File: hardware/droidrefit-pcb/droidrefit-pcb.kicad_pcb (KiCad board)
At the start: 2 copper layers, 100 x 70 mm, 30 parts, among them J1 USB-C 5V in, J2 SERVO SIG/+5V/GND, J3 NEOPIXEL JST-SH, J5 SPEAKER 4-8ohm, Q1 P-MOSFET revpol, U1 ESP32-DevKit-30, U2 DFPlayer-Mini, U3 74AHCT1G125

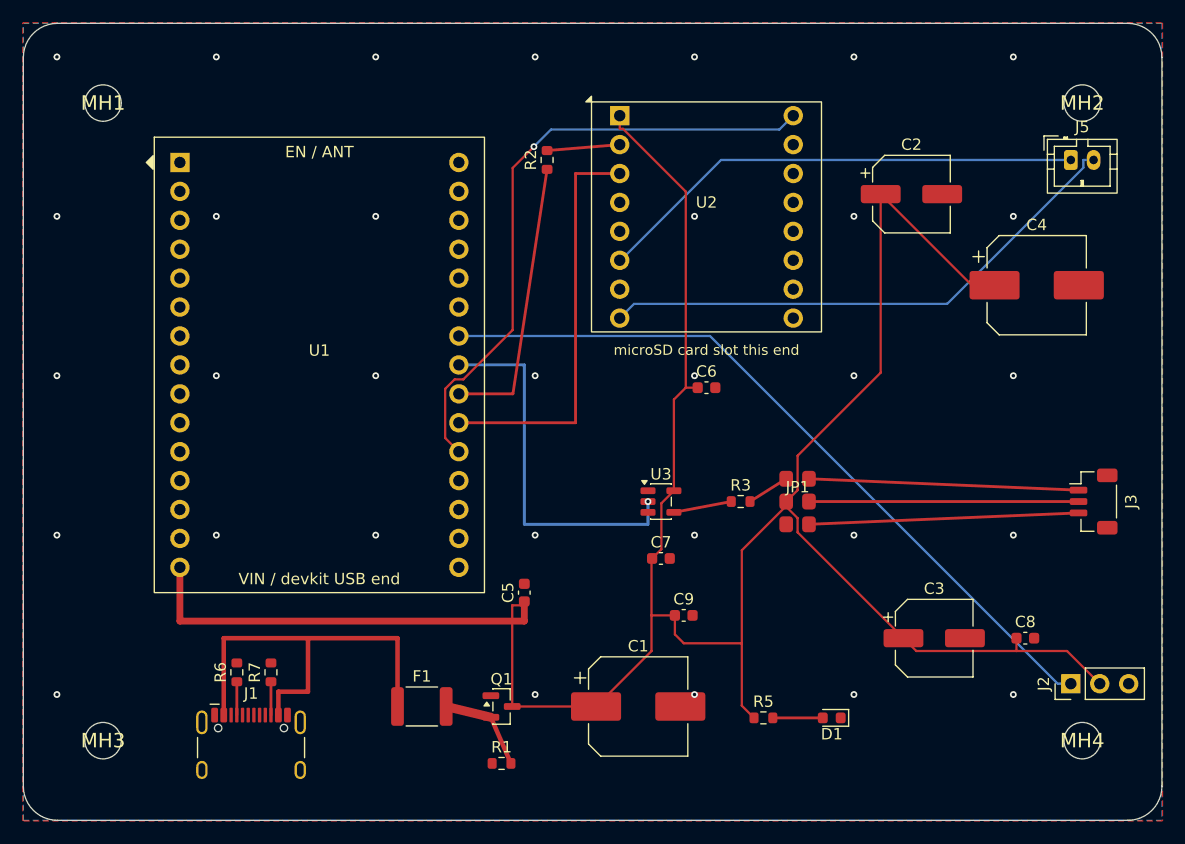
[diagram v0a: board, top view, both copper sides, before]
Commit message: PCB: add buttons/buzzer/OLED/UART headers, fix JP1 default pinout
droidrefit-pcb respin closing gaps DESIGN.md had already speced but never
drawn into the schematic/board:

- New J6 (BUTTONS, 1x4: GND/IO32/IO33/IO25), J7 (BUZZER, 1x2: IO27 via a
  new R8 100ohm series/GND), J8 (OLED I2C, 1x4: 3V3/GND/SDA/SCL, with new
  R9/R10 4.7k pull-ups to 3V3), J9 (UART0 ACCESS, 1x4: 3V3/GND/TX0/RX0).
  All four wired straight to U1's existing free socket pins per the pin
  assignments DESIGN.md's own Connectors/firmware-pin-map tables already
  committed to. All dnp+hand-solder like J2/J5 (2.54mm headers, not
  JLC-placed); R8/R9/R10 are real JLC-placed SMD 0603s.
- Fixed JP1 (NeoPixel pin-order solder-bridge field): shipped default was
  DIN-P1/V+-P2/GND-P3, but this session's NeoPixel bring-up empirically
  confirmed the real dome connector is GND-pin1/V+-pin2/Signal-pin3 -- DIN
  and GND were swapped from the shipped default. Remapped which J3 pin each
  bridge pad reaches so the same-row, no-cut default now matches reality.
- Board: placed + routed all new nets (mostly by hand, Freerouting for the
  denser fan-outs), GND pour refilled to pick up the new pads. ERC clean
  (0 errors, same 3 pre-existing symbol-mismatch warnings as before). DRC:
  down to 1 residual error (a zone-clearance short at JP1's own bare/DNP
  bridge-field pads, reproduced across multiple routing strategies -- looks
  like a zone-fill edge case in that one tightly-packed 6-pad SMD cluster,
  not a connectivity mistake; flagged in DESIGN.md/fab/README.md for a
  quick GUI nudge-and-refill before ordering) plus the same 13 pre-existing
  cosmetic warnings as before.
- Deleted the unused, never-instantiated 74xx:74AHCT125 (quad) and
  Connector:Barrel_Jack symbol-library leftovers from the schematic.
- Regenerated the full fab package (gerbers/drill/BOM-full/BOM-JLC/
  CPL-JLC/README) -- BOM-JLC/CPL-JLC now 16 lines/24 designators (was
  11/17). LCSC part numbers for R8/R9/R10 still TBD, not guessed her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
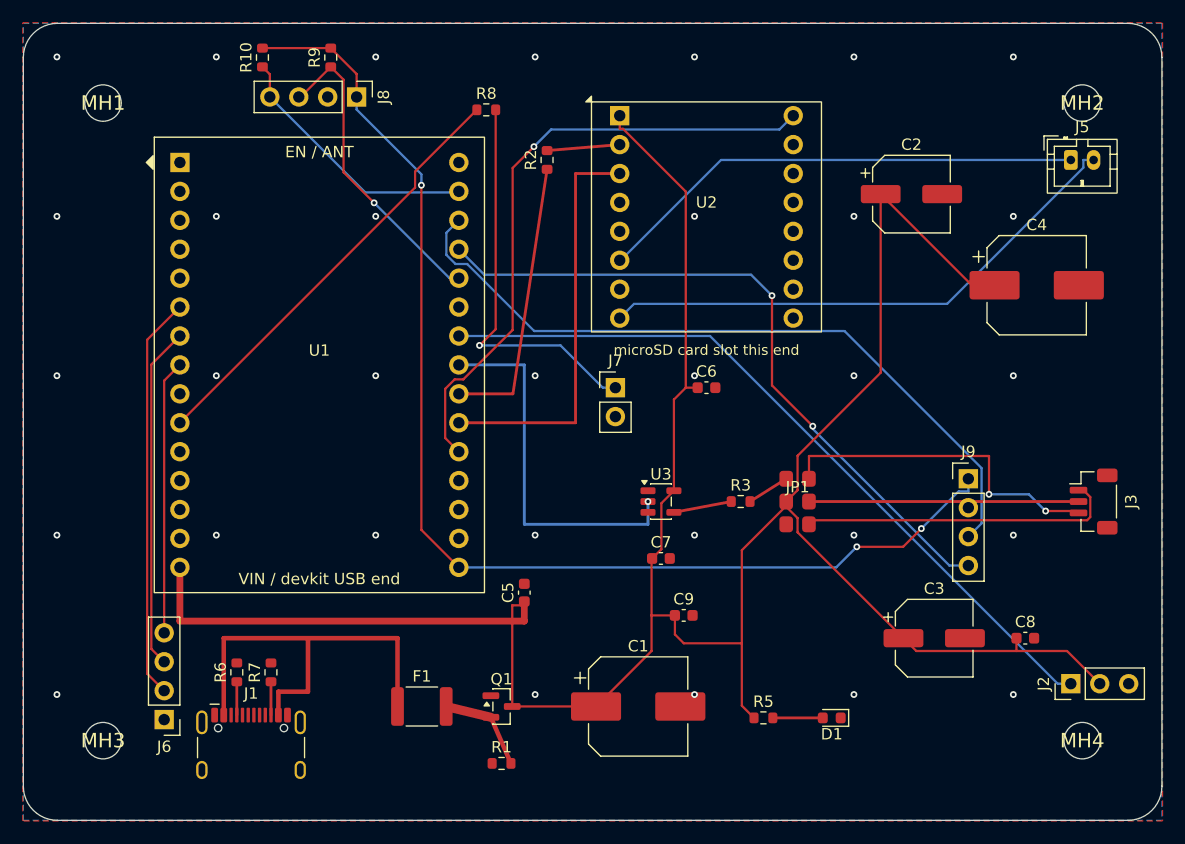
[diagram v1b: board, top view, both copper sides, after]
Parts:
- added J6: BUTTONS, Connector_PinHeader_2.54mm:PinHeader_1x04_P2.54mm_Vertical, F.Cu at (12.4, 61.1)
- added J7: BUZZER, Connector_PinHeader_2.54mm:PinHeader_1x02_P2.54mm_Vertical, F.Cu at (52.0, 32.0)
- added J8: OLED I2C, Connector_PinHeader_2.54mm:PinHeader_1x04_P2.54mm_Vertical, F.Cu at (29.3, 6.46)
- added J9: UART0 ACCESS, Connector_PinHeader_2.54mm:PinHeader_1x04_P2.54mm_Vertical, F.Cu at (83.0, 40.0)
- added R10: 4.7k, Resistor_SMD:R_0603_1608Metric, F.Cu at (21.0, 3.00)
- added R8: 100, Resistor_SMD:R_0603_1608Metric, F.Cu at (40.7, 7.60)
- added R9: 4.7k, Resistor_SMD:R_0603_1608Metric, F.Cu at (27.0, 3.00)
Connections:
- JP1 pad 4: NPX_P1 -> NPX_P3
- JP1 pad 6: NPX_P3 -> NPX_P1
- U1 pad 10: (no net) -> BUZZER_IO27
- U1 pad 17: (no net) -> I2C_SCL
- U1 pad 18: (no net) -> UART0_TX0
- U1 pad 19: (no net) -> UART0_RX0
- U1 pad 20: (no net) -> I2C_SDA
- U1 pad 30: +3V3 -> 3V3
- U1 pad 6: (no net) -> BTN_UP
- U1 pad 7: (no net) -> BTN_DOWN
- U1 pad 8: (no net) -> BTN_SND
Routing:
- net 3V3: track 0.00 -> 104.9 mm, vias 0 -> 3
- net UART0_TX0: track 0.00 -> 64.8 mm
- net UART0_RX0: track 0.00 -> 61.0 mm, vias 0 -> 2
- net BUZZER_IO27: track 0.00 -> 38.3 mm
- net BTN_UP: track 0.00 -> 35.5 mm
- net BUZZER_PWM: track 0.00 -> 34.8 mm, vias 0 -> 1
- net BTN_DOWN: track 0.00 -> 30.1 mm
- net I2C_SDA: track 0.00 -> 27.6 mm, vias 0 -> 1
- net BTN_SND: track 0.00 -> 24.1 mm
- net I2C_SCL: track 0.00 -> 23.0 mm
- net NPX_P3: track 23.7 -> 29.7 mm, vias 0 -> 2
- net NPX_P1: track 23.7 -> 28.0 mm

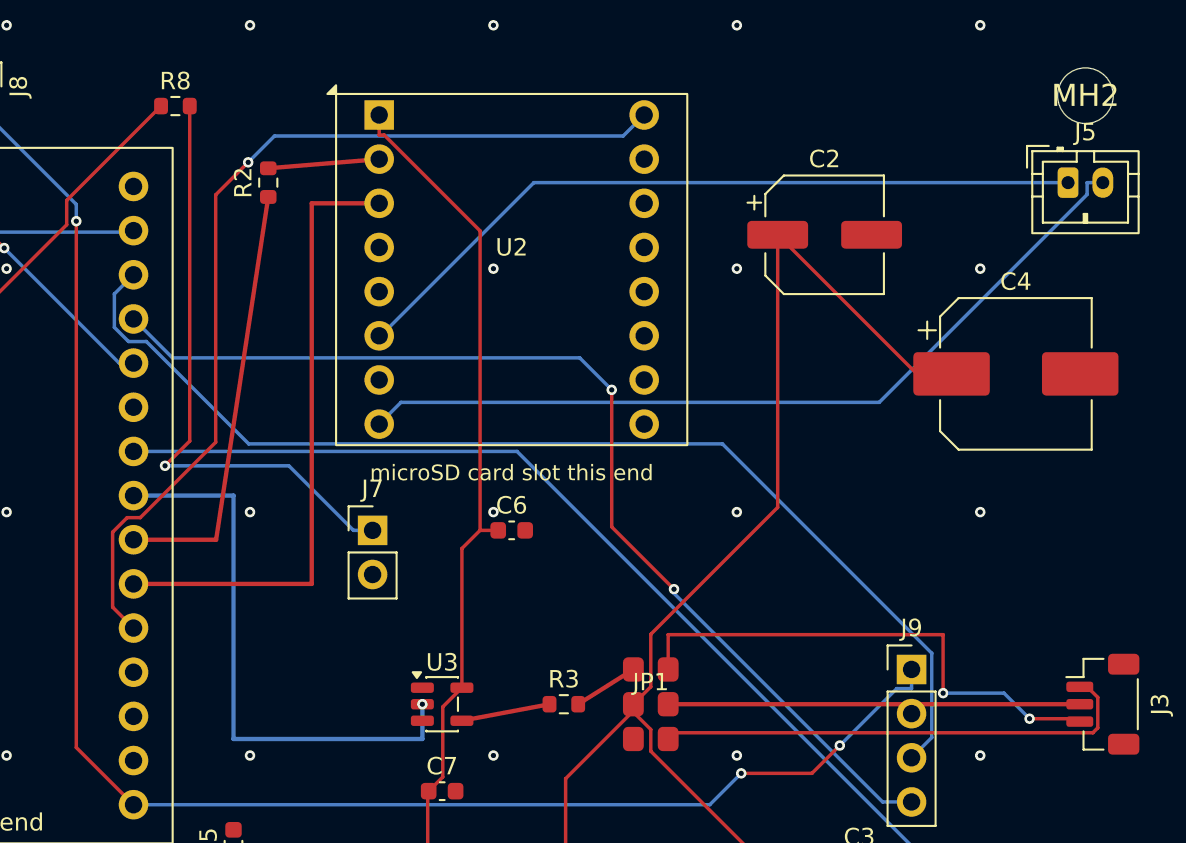
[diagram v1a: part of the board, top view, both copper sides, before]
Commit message: PCB: move J7 off the microSD card path, reroute NPX_P2 around J9 -> 0 DRC errors
Follow-up to the header respin, two fixes:

- J7 (buzzer header) was auto-placed at (52,32), directly in the DFPlayer's
  microSD card insertion/ejection path -- ~3mm south of the SD-slot edge,
  THT pins tall enough to foul a card or a plugged-in wire. Moved to
  (46.25,40), west of the card corridor; BUZZER_PWM re-routed.
- The residual GND/NPX_P2 DRC short was J9 sitting in the JP1->J3 NeoPixel
  bundle: the straight NPX_P2 run at y=42 clipped J9's GND pad at (83,42.54).
  Rerouting P1/P3 around J9 by hand earlier had left P2 straight through.
  Let Freerouting route NPX_P2 (as it already had for P1); that also
  cleared the JP1 bridge-field zone-clearance sliver.

Board is now 0 DRC errors + the same 12 pre-existing cosmetic warnings.
Fab package (gerbers/drill/zip/CPL) regenerated for the new J7 silk
position. BOM unchanged. R8/R9/R10 LCSC part numbers still TBD.

Co-Authored-By: Claude Sonnet 5 <noreply@anthropic.com>
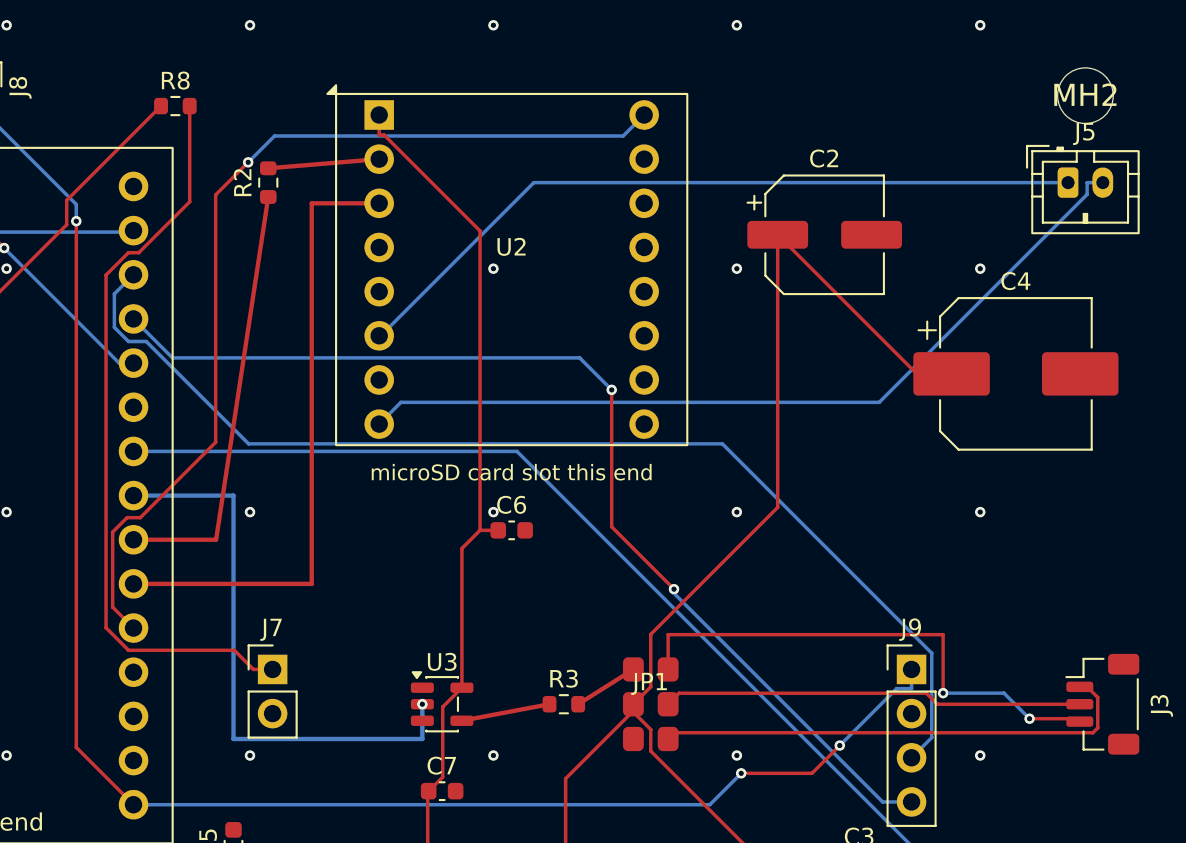
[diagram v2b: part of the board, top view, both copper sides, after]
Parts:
- moved J7 9.85 mm to (46.2, 40.0)
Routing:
- net BUZZER_PWM: track 34.8 -> 42.9 mm, vias 1 -> 0
- net NPX_P2: track 23.7 -> 24.2 mm

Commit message: PCB: move the 4 M3 mounting holes tighter into the corners
The 7mm-inset positions had MH2's keepout ring overlapping J5's courtyard
(a pre-existing body_overlap) and MH3/MH4 crowding the new J6 buttons
header / the J2 servo header -- an M3 screw + washer at those corners would
have fought a plugged-in connector.

Moved all 4 to a symmetric 91 x 61 mm pattern, 4.5 mm in from each edge
(4.5/4.5, 95.5/4.5, 4.5/65.5, 95.5/65.5). Now ~4mm clearance from a washer
edge to the nearest connector pad at every corner. All mechanical
overlaps gone; still 0 DRC errors. Enclosure is 3D-printed and designed
around the holes, so the asymmetry-vs-components tradeoff went to
clearance. Drill file + gerbers + zip regenerated.

Co-Authored-By: Claude Sonnet 5 <noreply@anthropic.com>
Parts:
- moved MH1 3.54 mm to (4.50, 4.50)
- moved MH2 3.54 mm to (95.5, 4.50)
- moved MH3 3.54 mm to (4.50, 65.5)
- moved MH4 3.54 mm to (95.5, 65.5)
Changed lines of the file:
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@@
 	(footprint "MountingHole:MountingHole_3.2mm"
 		(layer "F.Cu")
-		(at 7 63)
+		(at 4.5 65.5)
 		(property "Reference" "MH3"
 			(at 0 0 0)
@@
 	(footprint "MountingHole:MountingHole_3.2mm"
 		(layer "F.Cu")
-		(at 7 7)
+		(at 4.5 4.5)
 		(property "Reference" "MH1"
 			(at 0 0 0)
@@
 	(footprint "MountingHole:MountingHole_3.2mm"
 		(layer "F.Cu")
-		(at 93 7)
+		(at 95.5 4.5)
 		(property "Reference" "MH2"
 			(at 0 0 0)
@@
 	(footprint "MountingHole:MountingHole_3.2mm"
 		(layer "F.Cu")
-		(at 93 63)
+		(at 95.5 65.5)
 		(property "Reference" "MH4"
 			(at 0 0 0)

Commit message: PCB: explicit GND trace to J7 pin 2
KiCad GUI DRC flagged "Zone [GND] on F.Cu, priority 0 - missing
connections" -- J7's GND pad, now sitting in the dense U1<->U2 channel
after the SD-card-path move, isn't reliably reached by the GND pour on
either layer in that tight pocket (the swig-backend DRC didn't catch it;
the GUI's fill engine does). Added a short explicit GND trace from J7/2 to
C5/2 so it no longer depends on the pour squeezing in there.

Still 0 DRC errors here. Refill zones in the KiCad GUI (Edit -> Fill All
Zones / B) after opening -- the swig zone fill and KiCad 9's GUI fill
don't always agree, and the GUI's is authoritative.

Co-Authored-By: Claude Sonnet 5 <noreply@anthropic.com>
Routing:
- net GND: track 0.00 -> 7.05 mm
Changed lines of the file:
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@@
 		)
 		(property "Value" "MountingHole_3.2mm"
-			(at -4.5 -4.5 270)
+			(at 0 -15.5 270)
 			(layer "F.Fab")
 			(effects
@@
 		)
 		(property "Value" "MountingHole_3.2mm"
-			(at -5 6 90)
+			(at 0 14 90)
 			(layer "F.Fab")
 			(effects
@@
 		)
 		(property "Value" "MountingHole_3.2mm"
-			(at -5 -5 0)
+			(at -14 0 0)
 			(layer "F.Fab")
 			(effects
@@
 		)
 		(property "Value" "MountingHole_3.2mm"
-			(at -4 4.5 0)
+			(at -14 0 0)
 			(layer "F.Fab")
 			(effects
@@
 		(net "CC2")
 	)
+	(segment
+		(start 46.25 42.54)
+		(end 44 49.225)
+		(width 0.25)
+		(layer "F.Cu")
+		(net "GND")
+	)
 	(via

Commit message: PCB: GND stitching via to reconnect an isolated F.Cu pour island
kicad-cli DRC (--refill-zones, the same engine as the GUI) showed the real
issue behind the "Zone [GND] on F.Cu missing connections" the swig-backend
DRC kept missing: the F.Cu GND pour was fragmenting into islands. One
island, walled off by the VBUS_IN/CC1/CC2 traces around J1, held R6/R7's
GND pads (SMD, F.Cu-only) with no path back to the net. Added a GND
stitching via at (20.25,56) inside that island, tying it to the
continuous B.Cu GND pour.

kicad-cli DRC now: 0 errors, 0 unconnected items. Zone fill regenerated
with KiCad's own engine (--save-board) so the on-disk fill matches the GUI.
Remaining warnings are cosmetic (U2 lib descr, silk-over-pad on the
mounting holes) plus some kicad-cli-only "MountingHole not found" noise
that won't appear in the GUI (global lib table resolves it there).

Co-Authored-By: Claude Sonnet 5 <noreply@anthropic.com>
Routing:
- net GND: vias 32 -> 33
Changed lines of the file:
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@@
+	)
+	(via
+		(at 20.25 56)
+		(size 0.6)
+		(drill 0.3)
+		(layers "F.Cu" "B.Cu")
+		(net "GND")
 	)
 	(via
